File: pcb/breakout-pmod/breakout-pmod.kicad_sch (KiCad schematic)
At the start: 13 parts, among them J1 FX18-120P-0.8SV20

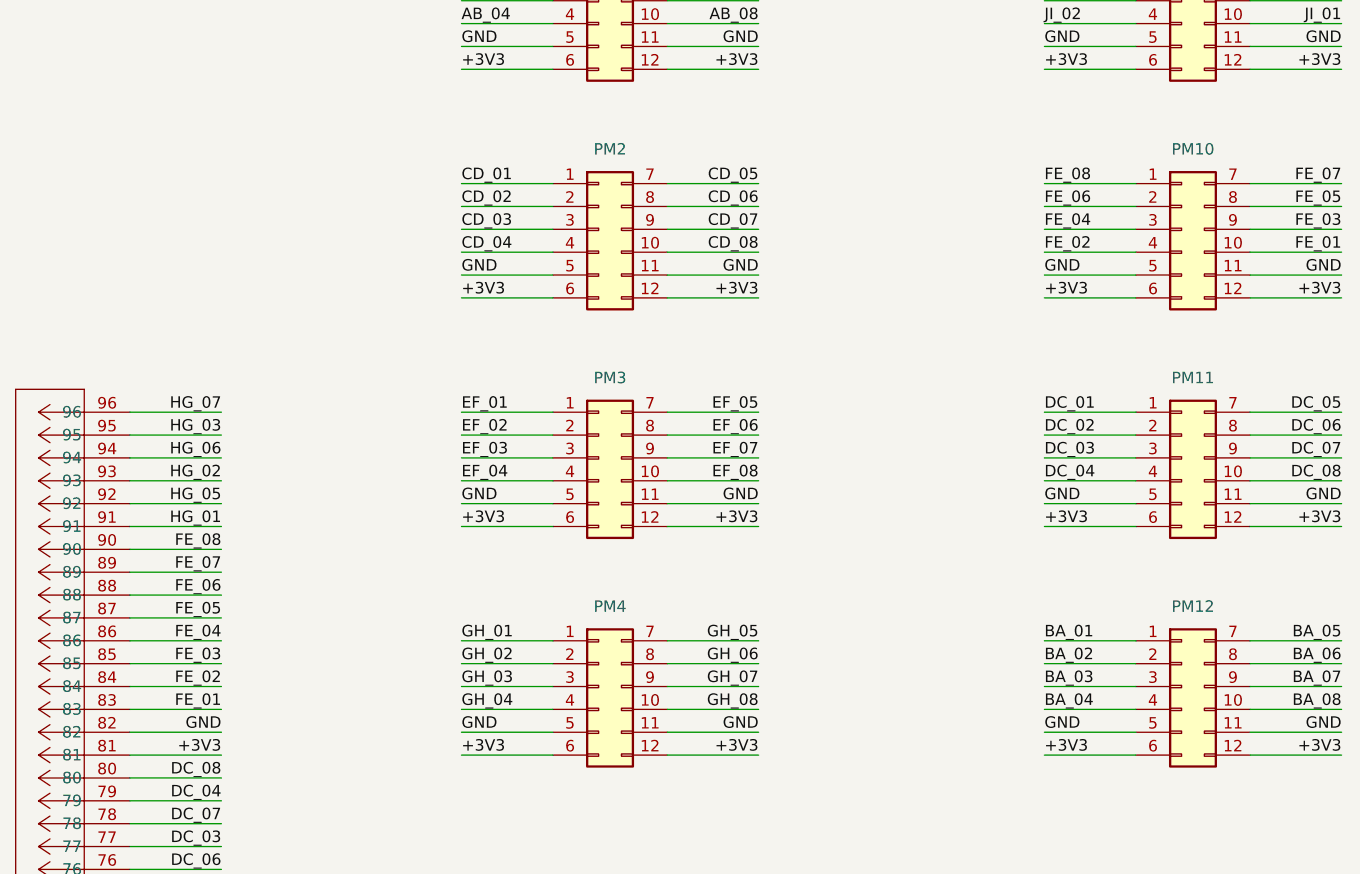
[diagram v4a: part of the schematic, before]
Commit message: [pmod] fix order of FE pmod
Note: this is actually wired backwards on the PCB
and probably won't mirror correctly.
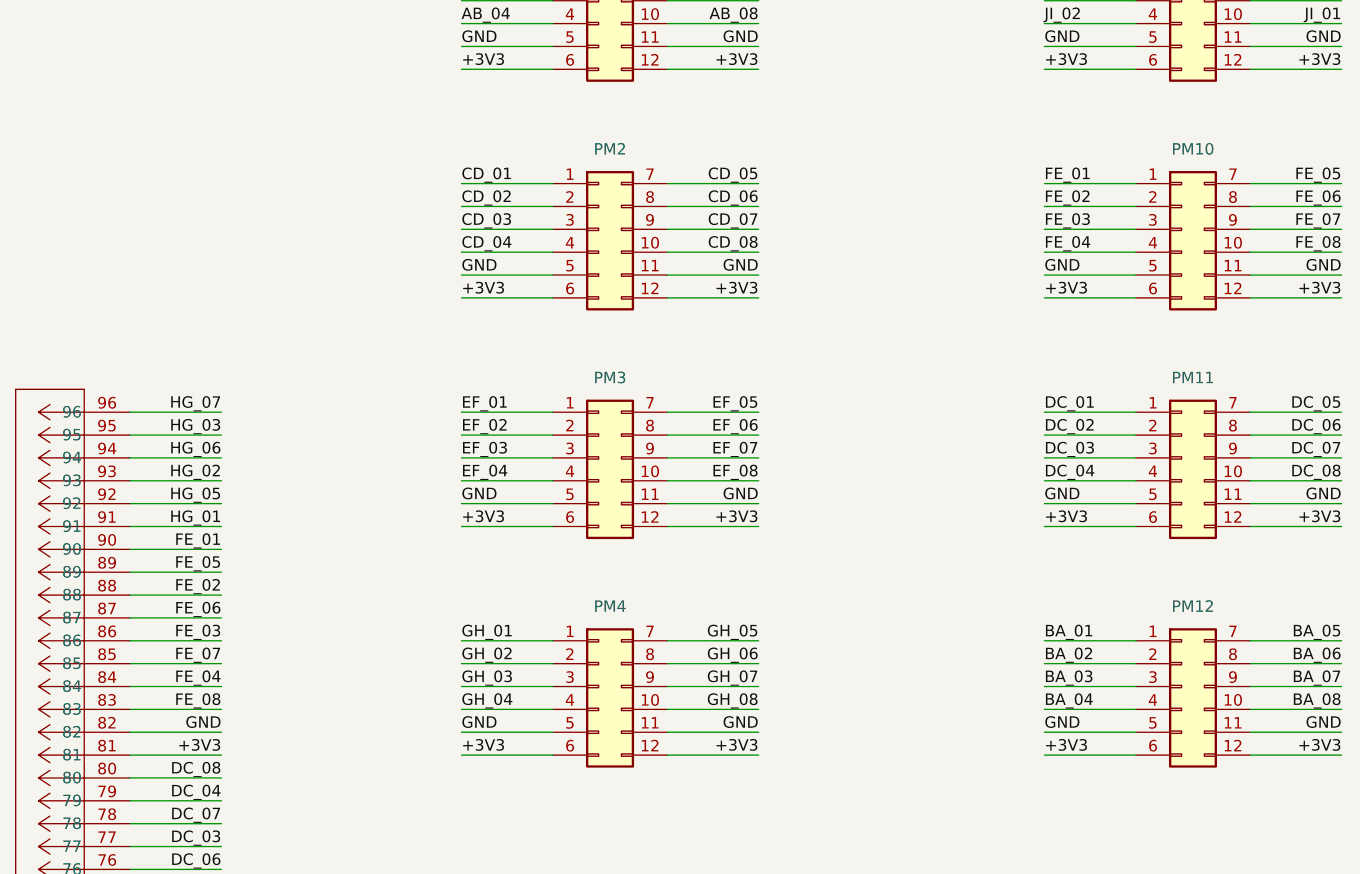
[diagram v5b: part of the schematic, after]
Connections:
- net FE_01: now also J1.90, PM10.1 (Pin_1); no longer J1.83, PM10.10 (Pin_10)
- net FE_02: now also J1.88, PM10.2 (Pin_2); no longer J1.84, PM10.4 (Pin_4)
- net FE_03: now also J1.86, PM10.3 (Pin_3); no longer J1.85, PM10.9 (Pin_9)
- net FE_04: now also J1.84, PM10.4 (Pin_4); no longer J1.86, PM10.3 (Pin_3)
- net FE_05: now also J1.89, PM10.7 (Pin_7); no longer J1.87, PM10.8 (Pin_8)
- net FE_06: now also J1.87, PM10.8 (Pin_8); no longer J1.88, PM10.2 (Pin_2)
- net FE_07: now also J1.85, PM10.9 (Pin_9); no longer J1.89, PM10.7 (Pin_7)
- net FE_08: now also J1.83, PM10.10 (Pin_10); no longer J1.90, PM10.1 (Pin_1)
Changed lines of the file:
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@@
 	)
 	(label "FE_07"
-		(at 138.43 107.95 180)
+		(at 138.43 118.11 180)
 		(fields_autoplaced yes)
 		(effects
@@
 	)
 	(label "FE_05"
-		(at 262.89 67.31 180)
+		(at 262.89 64.77 180)
 		(fields_autoplaced yes)
 		(effects
@@
 	)
 	(label "FE_07"
-		(at 262.89 64.77 180)
+		(at 262.89 69.85 180)
 		(fields_autoplaced yes)
 		(effects
@@
 	)
 	(label "FE_05"
-		(at 138.43 113.03 180)
+		(at 138.43 107.95 180)
 		(fields_autoplaced yes)
 		(effects
@@
 	)
 	(label "FE_02"
-		(at 138.43 120.65 180)
+		(at 138.43 110.49 180)
 		(fields_autoplaced yes)
 		(effects
@@
 	)
 	(label "FE_02"
-		(at 229.87 72.39 0)
+		(at 229.87 67.31 0)
 		(fields_autoplaced yes)
 		(effects
@@
 	)
 	(label "FE_08"
-		(at 138.43 105.41 180)
+		(at 138.43 123.19 180)
 		(fields_autoplaced yes)
 		(effects
@@
 	)
 	(label "FE_01"
-		(at 262.89 72.39 180)
-		(fields_autoplaced yes)
-		(effects
-			(font
-				(size 1.27 1.27)
-			)
-			(justify right bottom)
+		(at 229.87 64.77 0)
+		(fields_autoplaced yes)
+		(effects
+			(font
+				(size 1.27 1.27)
+			)
+			(justify left bottom)
 		)
 	)
@@
 	)
 	(label "FE_03"
-		(at 138.43 118.11 180)
+		(at 138.43 115.57 180)
 		(fields_autoplaced yes)
 		(effects
@@
 	)
 	(label "FE_04"
-		(at 138.43 115.57 180)
+		(at 138.43 120.65 180)
 		(fields_autoplaced yes)
 		(effects
@@
 	)
 	(label "FE_08"
-		(at 229.87 64.77 0)
-		(fields_autoplaced yes)
-		(effects
-			(font
-				(size 1.27 1.27)
-			)
-			(justify left bottom)
+		(at 262.89 72.39 180)
+		(fields_autoplaced yes)
+		(effects
+			(font
+				(size 1.27 1.27)
+			)
+			(justify right bottom)
 		)
 	)
@@
 	)
 	(label "FE_06"
-		(at 138.43 110.49 180)
+		(at 138.43 113.03 180)
 		(fields_autoplaced yes)
 		(effects
@@
 	)
 	(label "FE_03"
-		(at 262.89 69.85 180)
-		(fields_autoplaced yes)
-		(effects
-			(font
-				(size 1.27 1.27)
-			)
-			(justify right bottom)
+		(at 229.87 69.85 0)
+		(fields_autoplaced yes)
+		(effects
+			(font
+				(size 1.27 1.27)
+			)
+			(justify left bottom)
 		)
 	)
@@
 	)
 	(label "FE_04"
-		(at 229.87 69.85 0)
+		(at 229.87 72.39 0)
 		(fields_autoplaced yes)
 		(effects
@@
 	)
 	(label "FE_01"
-		(at 138.43 123.19 180)
+		(at 138.43 105.41 180)
 		(fields_autoplaced yes)
 		(effects
@@
 	)
 	(label "FE_06"
-		(at 229.87 67.31 0)
-		(fields_autoplaced yes)
-		(effects
-			(font
-				(size 1.27 1.27)
-			)
-			(justify left bottom)
-		)
-	)
+		(at 262.89 67.31 180)
+		(fields_autoplaced yes)
+		(effects
+			(font
+				(size 1.27 1.27)
+			)
+			(justify right bottom)
+		)
+	)

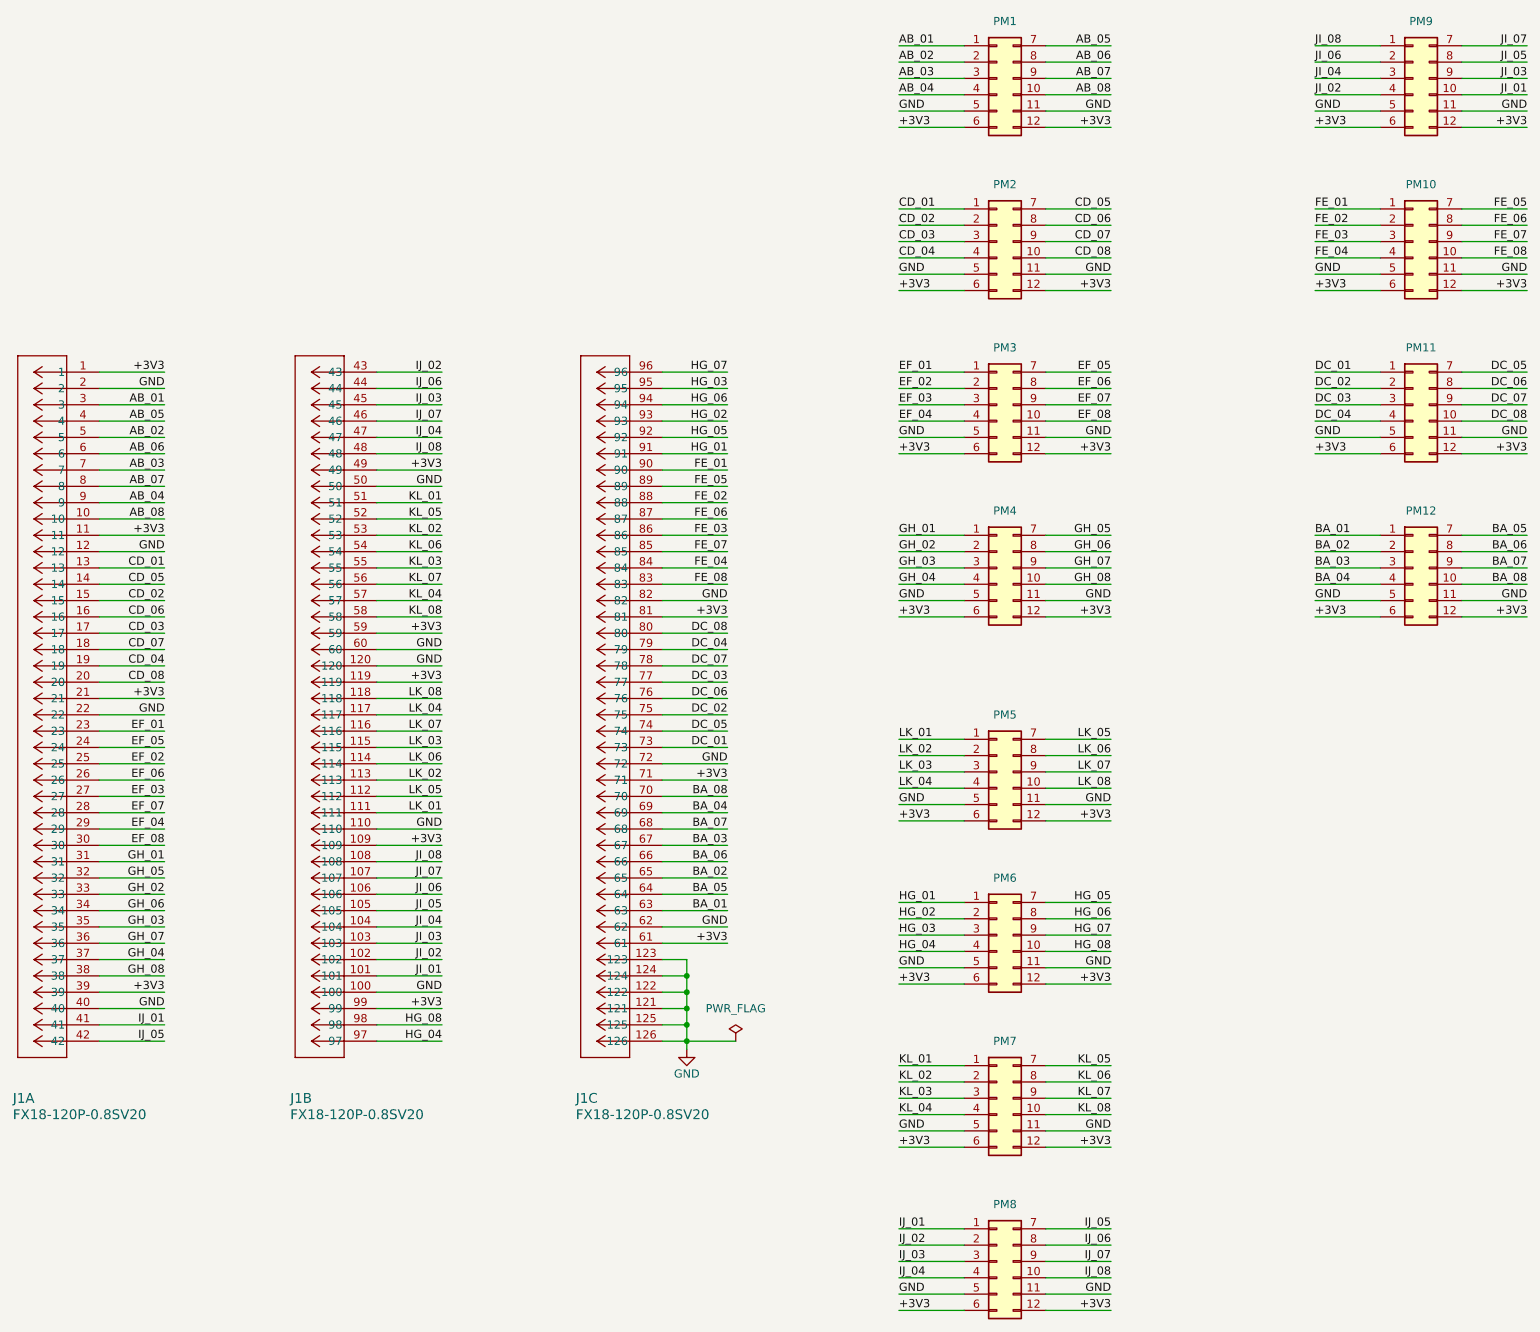
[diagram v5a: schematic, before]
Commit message: [pmod] fix order of JI pmod
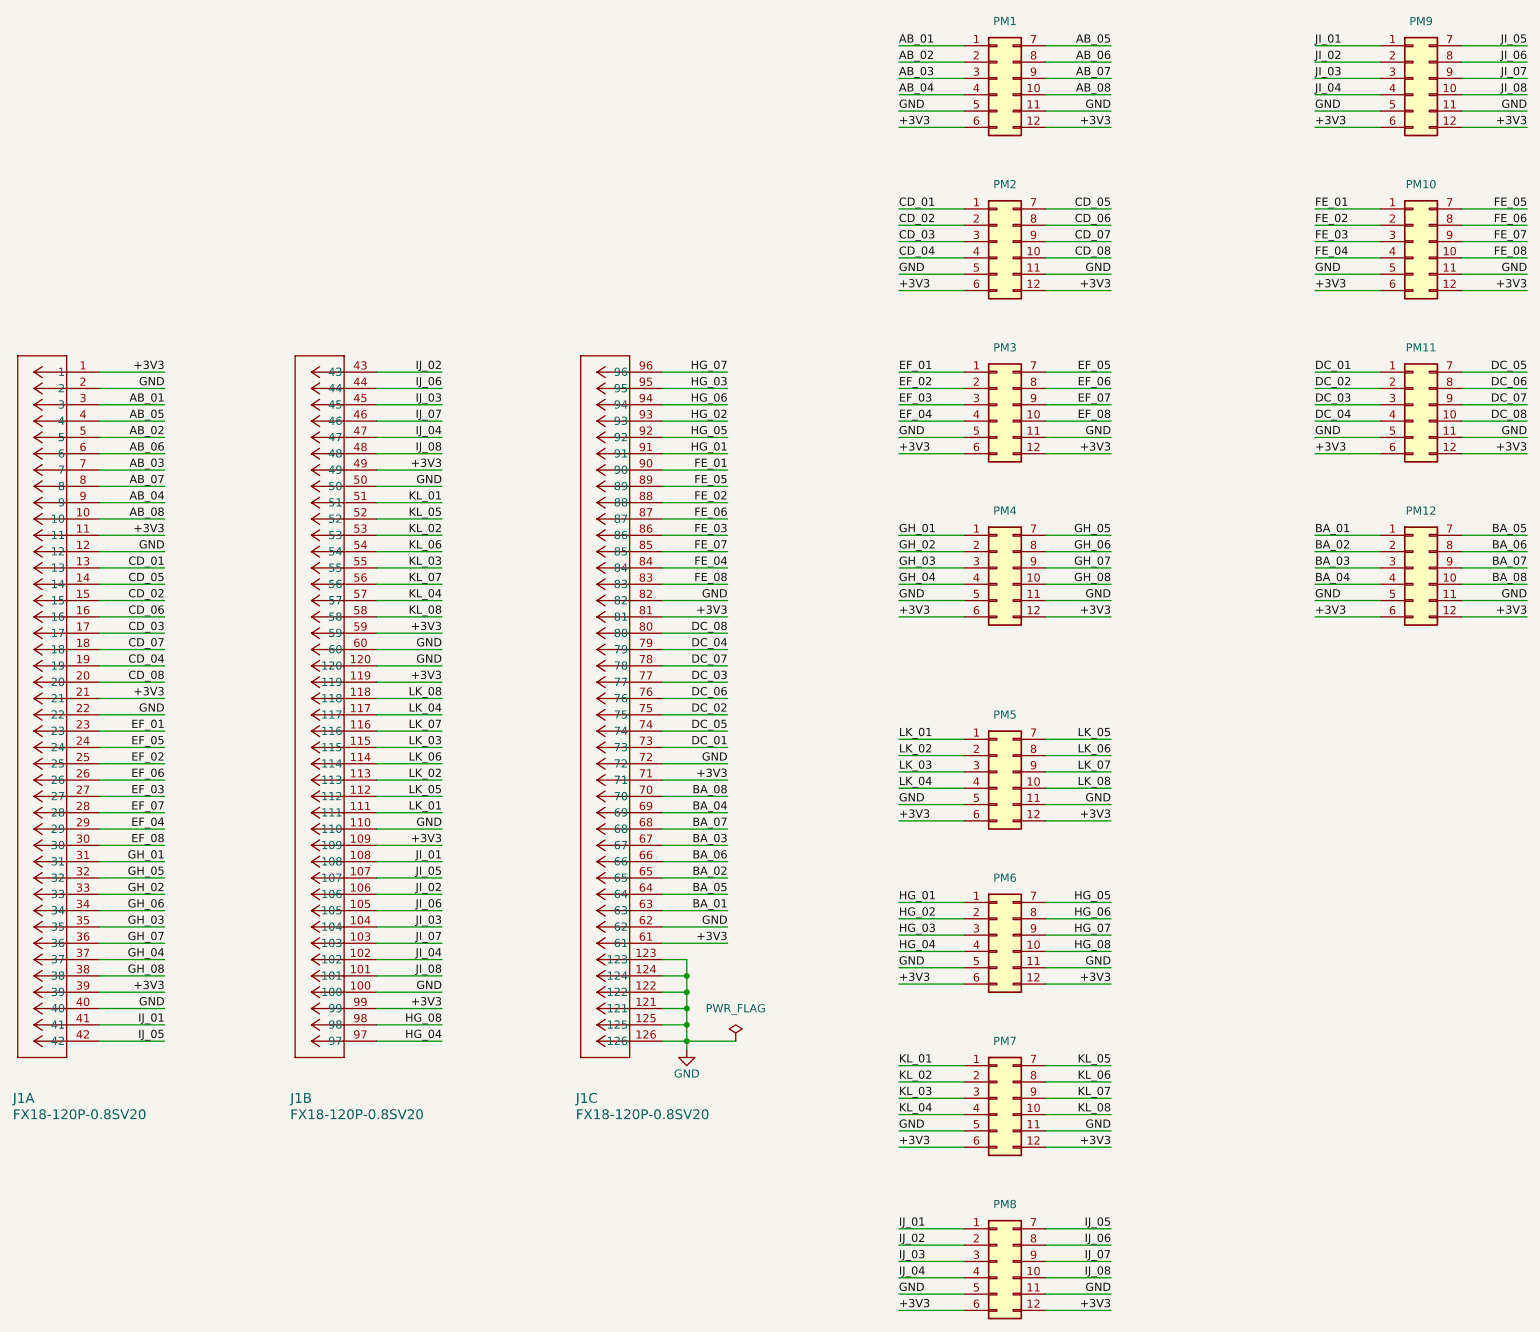
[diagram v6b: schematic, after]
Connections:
- net JI_01: now also J1.108, PM9.1 (Pin_1); no longer J1.101, PM9.10 (Pin_10)
- net JI_02: now also J1.106, PM9.2 (Pin_2); no longer J1.102, PM9.4 (Pin_4)
- net JI_03: now also J1.104, PM9.3 (Pin_3); no longer J1.103, PM9.9 (Pin_9)
- net JI_04: now also J1.102, PM9.4 (Pin_4); no longer J1.104, PM9.3 (Pin_3)
- net JI_05: now also J1.107, PM9.7 (Pin_7); no longer J1.105, PM9.8 (Pin_8)
- net JI_06: now also J1.105, PM9.8 (Pin_8); no longer J1.106, PM9.2 (Pin_2)
- net JI_07: now also J1.103, PM9.9 (Pin_9); no longer J1.107, PM9.7 (Pin_7)
- net JI_08: now also J1.101, PM9.10 (Pin_10); no longer J1.108, PM9.1 (Pin_1)
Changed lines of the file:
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@@
 	)
 	(label "JI_04"
-		(at 93.98 176.53 180)
+		(at 93.98 181.61 180)
 		(fields_autoplaced yes)
 		(effects
@@
 	)
 	(label "JI_06"
-		(at 93.98 171.45 180)
+		(at 93.98 173.99 180)
 		(fields_autoplaced yes)
 		(effects
@@
 	)
 	(label "JI_07"
-		(at 93.98 168.91 180)
+		(at 93.98 179.07 180)
 		(fields_autoplaced yes)
 		(effects
@@
 	)
 	(label "JI_03"
-		(at 262.89 44.45 180)
-		(fields_autoplaced yes)
-		(effects
-			(font
-				(size 1.27 1.27)
-			)
-			(justify right bottom)
+		(at 229.87 44.45 0)
+		(fields_autoplaced yes)
+		(effects
+			(font
+				(size 1.27 1.27)
+			)
+			(justify left bottom)
 		)
 	)
@@
 	)
 	(label "JI_08"
-		(at 93.98 166.37 180)
+		(at 93.98 184.15 180)
 		(fields_autoplaced yes)
 		(effects
@@
 	)
 	(label "JI_04"
-		(at 229.87 44.45 0)
+		(at 229.87 46.99 0)
 		(fields_autoplaced yes)
 		(effects
@@
 	)
 	(label "JI_08"
-		(at 229.87 39.37 0)
-		(fields_autoplaced yes)
-		(effects
-			(font
-				(size 1.27 1.27)
-			)
-			(justify left bottom)
+		(at 262.89 46.99 180)
+		(fields_autoplaced yes)
+		(effects
+			(font
+				(size 1.27 1.27)
+			)
+			(justify right bottom)
 		)
 	)
 	(label "JI_01"
-		(at 93.98 184.15 180)
+		(at 93.98 166.37 180)
 		(fields_autoplaced yes)
 		(effects
@@
 	)
 	(label "JI_02"
-		(at 93.98 181.61 180)
+		(at 93.98 171.45 180)
 		(fields_autoplaced yes)
 		(effects
@@
 	)
 	(label "JI_01"
-		(at 262.89 46.99 180)
-		(fields_autoplaced yes)
-		(effects
-			(font
-				(size 1.27 1.27)
-			)
-			(justify right bottom)
+		(at 229.87 39.37 0)
+		(fields_autoplaced yes)
+		(effects
+			(font
+				(size 1.27 1.27)
+			)
+			(justify left bottom)
 		)
 	)
@@
 	)
 	(label "JI_02"
-		(at 229.87 46.99 0)
+		(at 229.87 41.91 0)
 		(fields_autoplaced yes)
 		(effects
@@
 	)
 	(label "JI_05"
-		(at 262.89 41.91 180)
+		(at 262.89 39.37 180)
 		(fields_autoplaced yes)
 		(effects
@@
 	)
 	(label "JI_07"
-		(at 262.89 39.37 180)
+		(at 262.89 44.45 180)
 		(fields_autoplaced yes)
 		(effects
@@
 	)
 	(label "JI_05"
-		(at 93.98 173.99 180)
+		(at 93.98 168.91 180)
 		(fields_autoplaced yes)
 		(effects
@@
 	)
 	(label "JI_03"
-		(at 93.98 179.07 180)
+		(at 93.98 176.53 180)
 		(fields_autoplaced yes)
 		(effects
@@
 	)
 	(label "JI_06"
-		(at 229.87 41.91 0)
-		(fields_autoplaced yes)
-		(effects
-			(font
-				(size 1.27 1.27)
-			)
-			(justify left bottom)
-		)
-	)
+		(at 262.89 41.91 180)
+		(fields_autoplaced yes)
+		(effects
+			(font
+				(size 1.27 1.27)
+			)
+			(justify right bottom)
+		)
+	)
